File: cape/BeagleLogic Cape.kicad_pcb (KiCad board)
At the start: 2 copper layers, 54.6 x 70.9 mm, 22 parts, among them P1 CONN_02X14, Q1 BSS138, U1 bbb, U2 74LVCH16245, U3 EEPROM

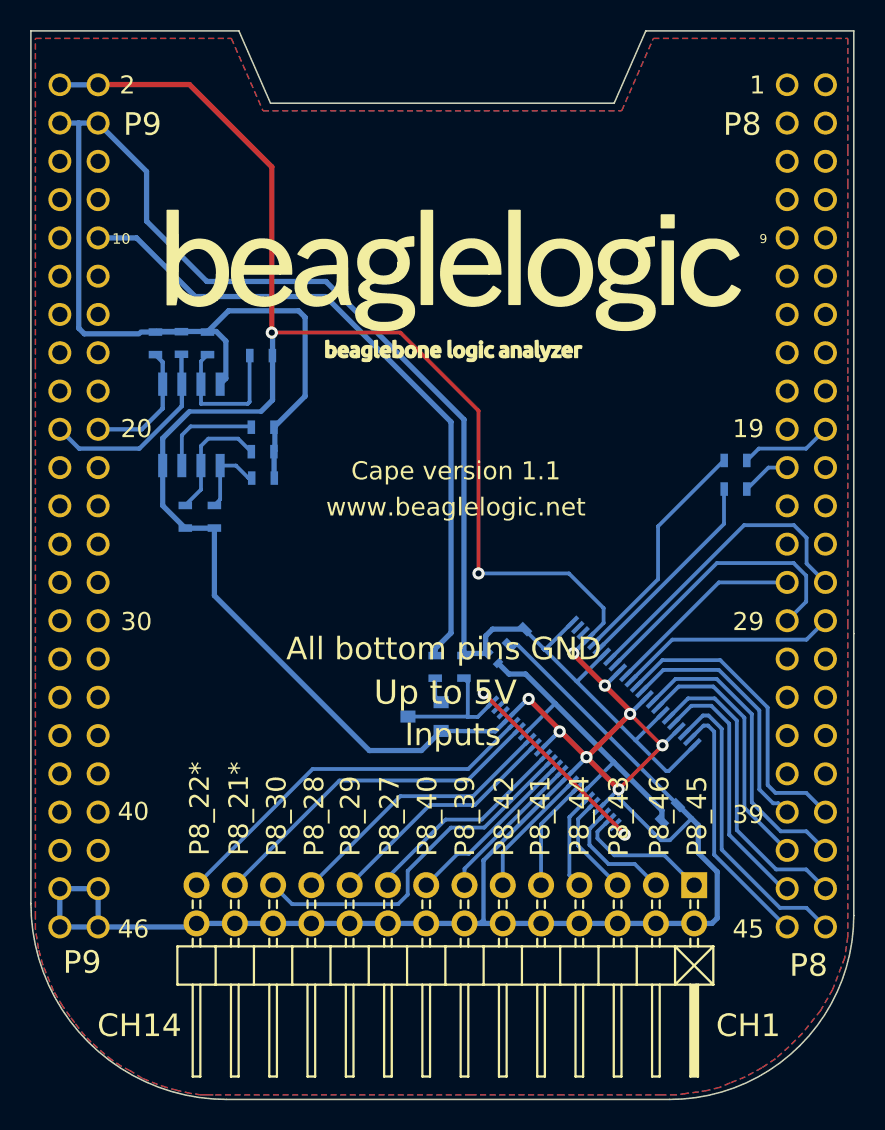
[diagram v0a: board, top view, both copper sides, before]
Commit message: update schema, pcb to kicad5 libs
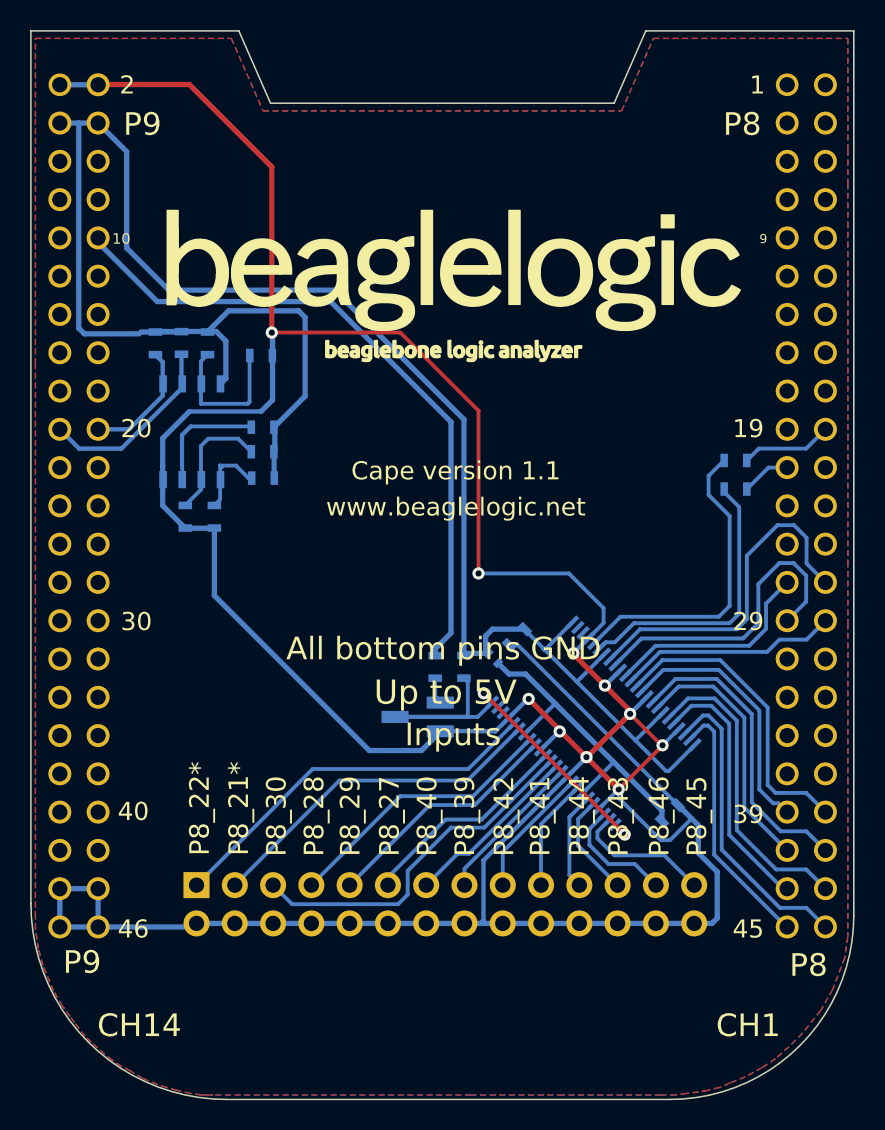
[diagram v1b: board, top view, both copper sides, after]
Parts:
- removed P1: CONN_02X14, Pin_Headers:Pin_Header_Angled_2x14
- removed Q1: BSS138, SMD_Packages:SOT-23
- removed U3: EEPROM, Housings_SOIC:SOIC-8_3.9x4.9mm_Pitch1.27mm
- added J101: Conn_02x14_Odd_Even, Pin_Headers:Pin_Header_Angled_2x14, B.Cu at (125.8, 115.7)
- added Q101: BSS138, Housings_SOT-23_SOT-143_TSOT-6:SOT-23_Handsoldering, B.Cu at (140.5, 104.5)
- added U101: AT24CS64-SSHM, SMD_Packages:SOIC-8-N, B.Cu at (125.5, 85.6)
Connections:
- net +3.3V renamed +3V3
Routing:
- net Net-(R8-Pad1): track 15.7 -> 20.7 mm
- net Net-(R9-Pad1): track 14.0 -> 18.9 mm
- net Net-(Q101-Pad3): track 23.7 -> 28.6 mm
- net Net-(R5-Pad1): track 6.90 -> 10.7 mm
- net /CH11: track 21.2 -> 23.6 mm
- net +3V3: track 129.5 -> 131.3 mm
- net /CH10: track 19.3 -> 20.8 mm
- net /CH9: track 13.3 -> 14.2 mm
- net /EP_SCL: track 13.2 -> 12.5 mm
